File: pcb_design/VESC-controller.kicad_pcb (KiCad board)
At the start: 4 copper layers, 160 x 90 mm, 257 parts, among them J1 GATE_DRIVER_CONN_U, J2 GATE_DRIVER_CONN_V, J3 GATE_DRIVER_CONN_W, J4 micro USB, J5 ACCEL, J6 REGEN, J7 12V, J8 V_BUS, J9 SWD, P1 HALL/Encoder, P101 CANBUS, P2 Resolver, P3 PWR_COMM, Q1 BSC340N08, U1 STM32F40X_LQFP64, U10 LM2903-SO8, U11 LM3488, U12 OPA2376AID, U13 LM1117IMP-v.v, U14 OPA2376AID, U16 OPA2376AID, U17 LM2903-SO8, U2 ISO1050, U3 OPA2376AID, U4 LM2903-SO8, U5 7400-TSSOP, U6 SN74ALVC08PWR, U7 SN74ALVC08PWR, U8 SN74AUP1G74, U9 LM22676QTJ-5.0, X2 ABM3B - 8MHz

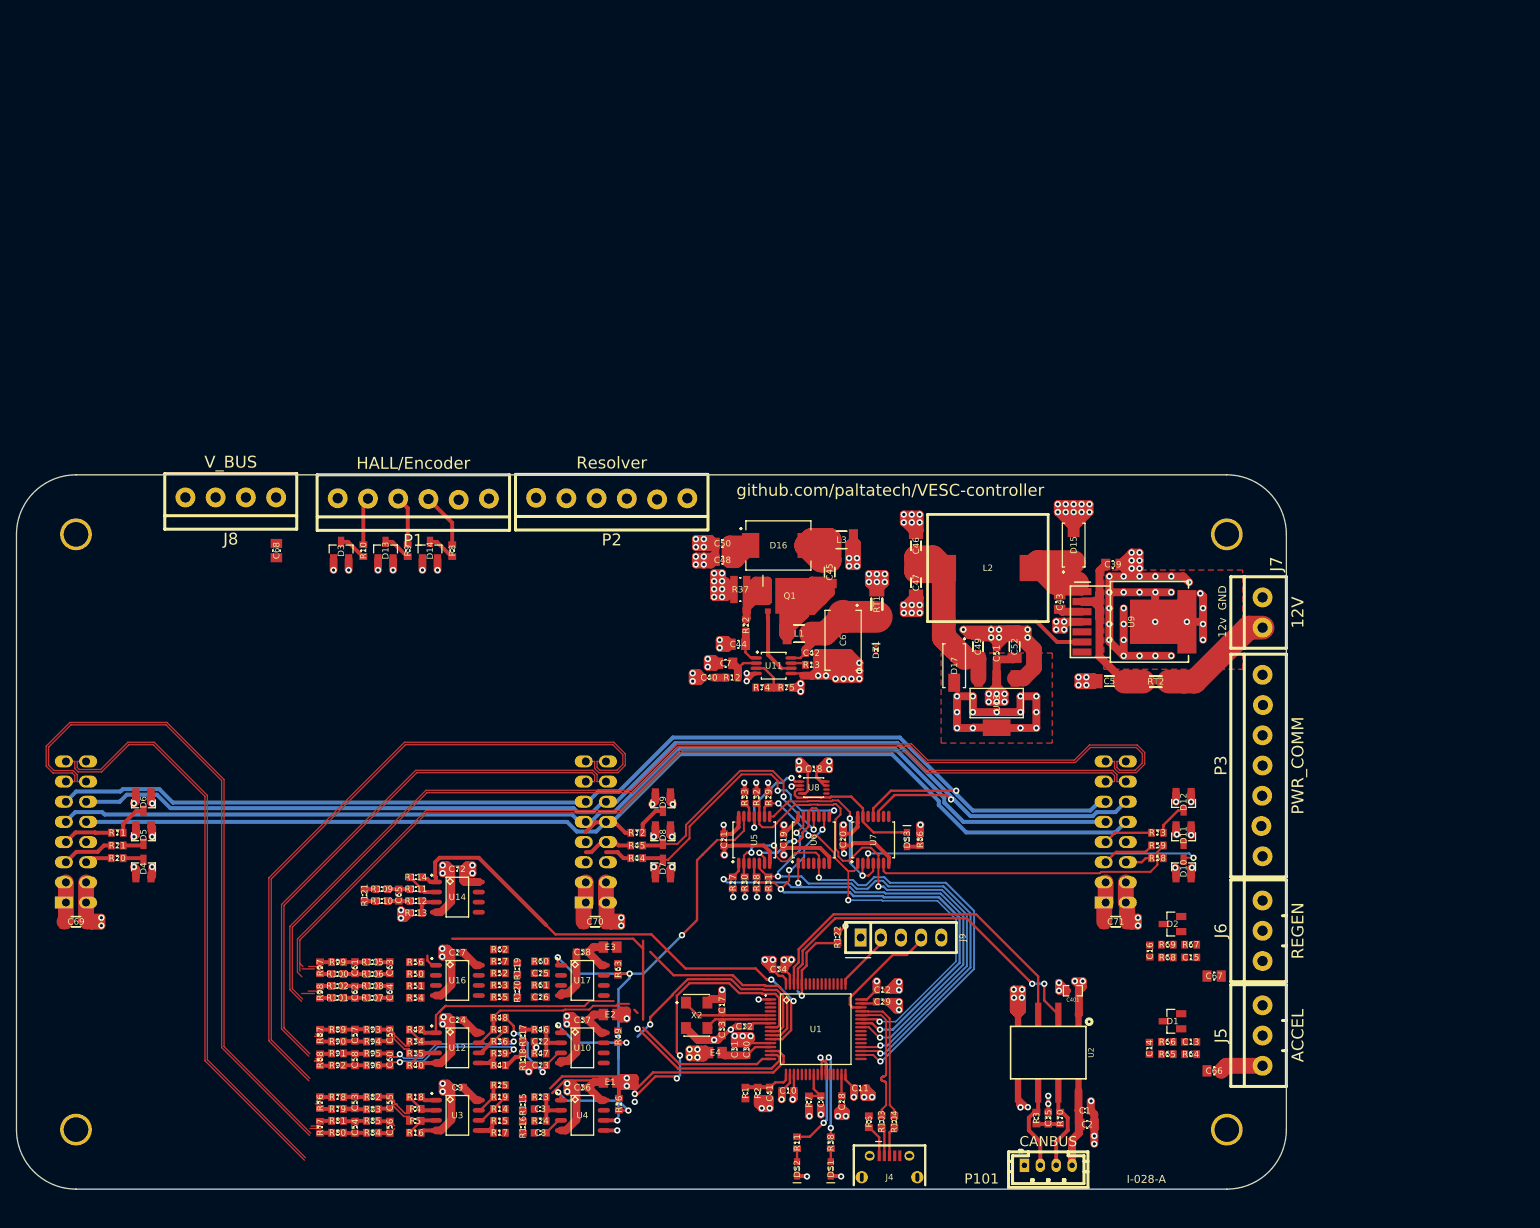
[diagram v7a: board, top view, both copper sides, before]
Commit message: More layout. Changed LED pin. Added placeholder for a resolver IC
Signed-off-by: Marcos Chaparro <mchaparro@paltatech.com>
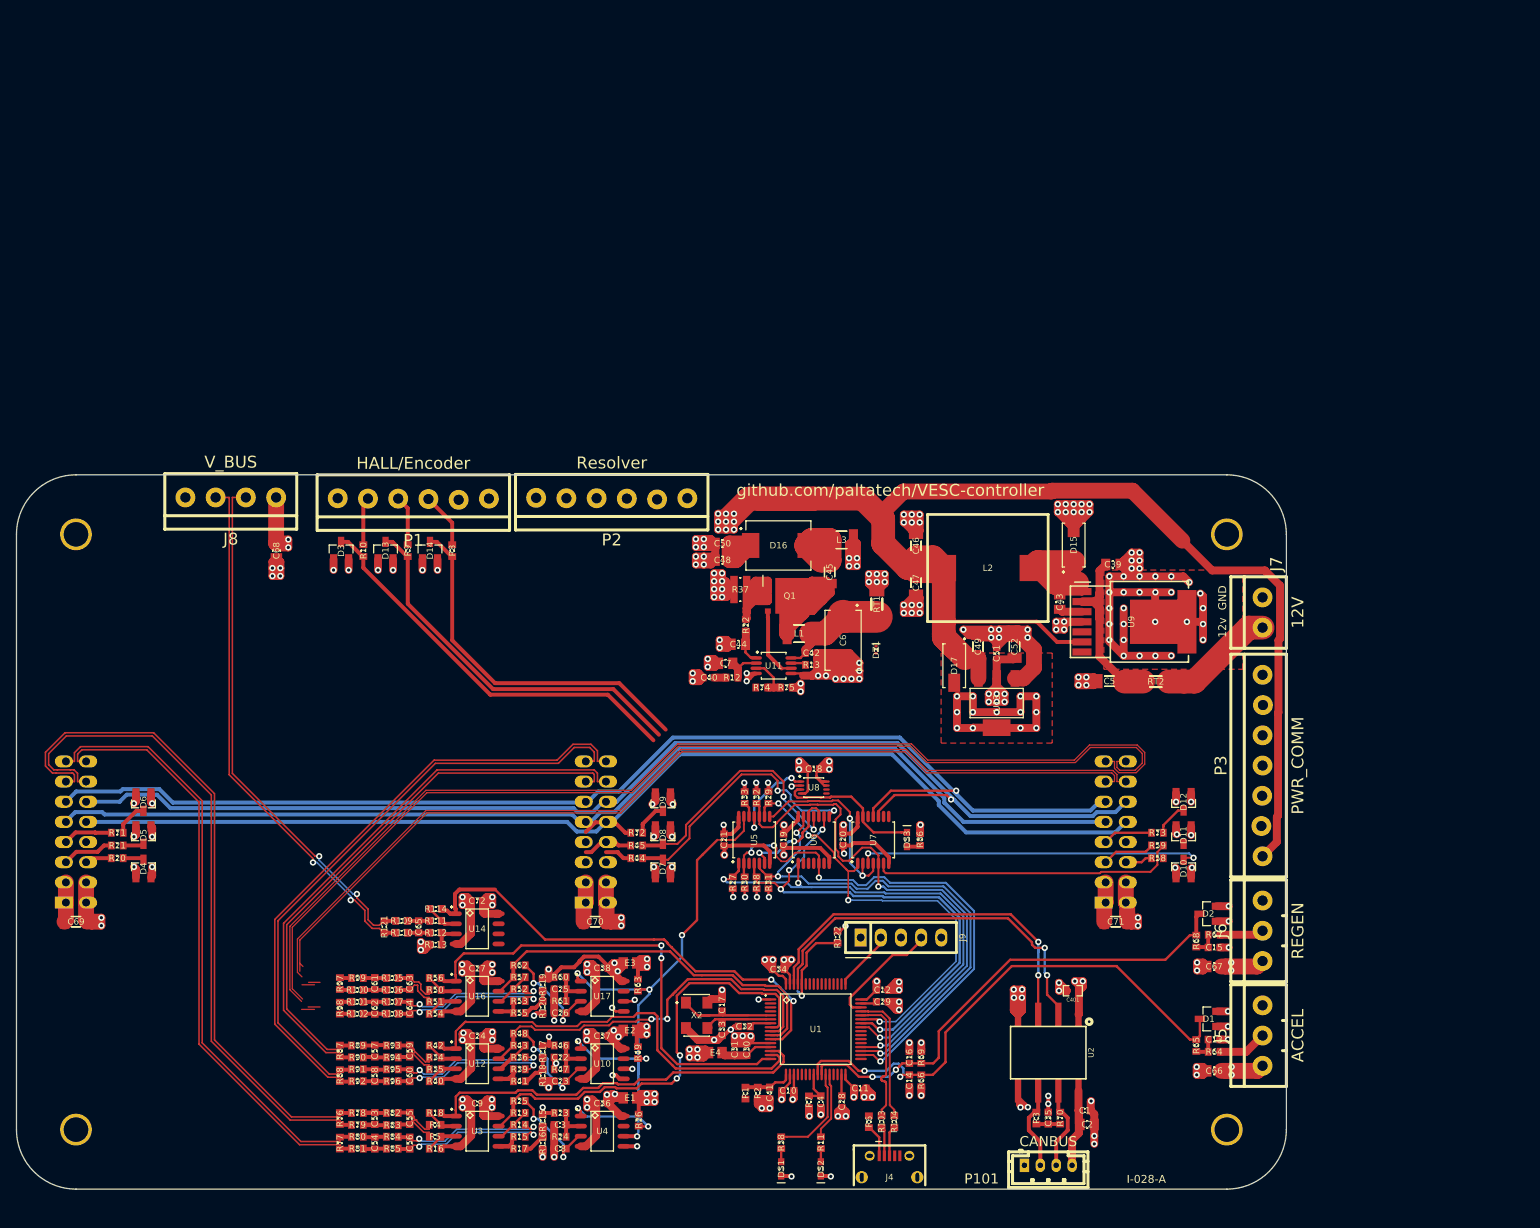
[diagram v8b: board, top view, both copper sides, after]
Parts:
- RT1: value POLYFUSE-30R500 -> POLYFUSE 5A
- RT2: value POLYFUSE-30R500 -> POLYFUSE- 2A
- moved R69 34.1 mm to (34.0, 28.4), turned to 270 degrees
- moved C16 33.1 mm to (32.5, 28.4)
- moved R66 31.4 mm to (34.0, 31.4), turned to 90 degrees
- moved C14 30.5 mm to (32.5, 31.4), turned to 270 degrees
- moved DS1 6.25 mm to (16.4, 42.5)
- moved R38 6.25 mm to (16.4, 39.1)
- moved C72 4.72 mm to (-22.0, 8.68)
- moved C65 4.72 mm to (-29.3, 11.9)
- moved R109 4.72 mm to (-31.5, 11.2)
- moved R110 4.72 mm to (-31.5, 12.7)
- moved R111 4.72 mm to (-27.2, 11.2)
- moved R112 4.72 mm to (-27.2, 12.7)
- moved R113 4.72 mm to (-27.2, 14.2)
- moved R114 4.72 mm to (-27.2, 9.70)
- moved R121 4.72 mm to (-33.6, 11.9)
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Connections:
- net /TX_SDA renamed /STM32F4/RX_SDA_NSS
- net Net-(P2-Pad1) renamed /resolver/COS-
- net Net-(P2-Pad2) renamed /resolver/COS+
- net Net-(P2-Pad3) renamed /resolver/SIN-
- net Net-(P2-Pad4) renamed /resolver/SIN+
- net Net-(P2-Pad5) renamed /resolver/EXC-
- net Net-(P2-Pad6) renamed /resolver/EXC+
- C14 pad 1: /Accel input conditioning/OUT -> /STM32F4/ADC_15
- C16 pad 1: /STM32F4/ADC_15 -> /STM32F4/ADC_8
- D1 pad 2: VCC -> +3.3
- D1 pad 3: /Accel input conditioning/OUT -> /STM32F4/ADC_15
- D2 pad 2: VCC -> +3.3
- D2 pad 3: /STM32F4/ADC_15 -> /STM32F4/ADC_8
- R65 pad 1: /Accel input conditioning/OUT -> /STM32F4/ADC_15
- R66 pad 2: /Accel input conditioning/OUT -> /STM32F4/ADC_15
- R68 pad 1: /STM32F4/ADC_15 -> /STM32F4/ADC_8
- R69 pad 2: /STM32F4/ADC_15 -> /STM32F4/ADC_8
- U1 pad 26: /STM32F4/LED_GREEN -> /STM32F4/ADC_8
- U1 pad 28: Net-(U1-Pad28) -> /STM32F4/LED_GREEN
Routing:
- net +5: track 52.0 -> 335.5 mm, vias 0 -> 15
- net /STM32F4/ADC_15: track 0.00 -> 66.7 mm, vias 0 -> 2
- net /V_bus-: track 1.42 -> 67.2 mm, vias 0 -> 2
- net /V_bus+: track 1.42 -> 66.6 mm, vias 0 -> 2
- net /STM32F4/ADC_8: track 0.00 -> 61.2 mm, vias 0 -> 2
- net /conditioning U/3.3V_AN: track 7.41 -> 57.0 mm, vias 0 -> 5
- net /Filters/HALL3_OUT: track 3.57 -> 50.5 mm
- net /Filters/HALL2_OUT: track 3.57 -> 48.0 mm
- net GND: track 528.3 -> 571.5 mm, vias 183 -> 207
- net /Filters/HALL1_OUT: track 3.57 -> 45.7 mm
- net /conditioning W/V_phase: track 20.2 -> 59.6 mm, vias 0 -> 2
- net /conditioning W/3.3V_AN: track 7.41 -> 46.4 mm, vias 0 -> 5
- net (no net): track 34.5 -> 6.71 mm
- net /conditioning V/3.3V_AN: track 9.17 -> 36.7 mm, vias 0 -> 5
- net /conditioning W/I_phase: track 26.9 -> 49.0 mm
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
